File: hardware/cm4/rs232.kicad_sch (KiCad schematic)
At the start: 13 parts, among them J3 D340 PC (4P4C), U3 ADuM5211, U5 MAX3232E

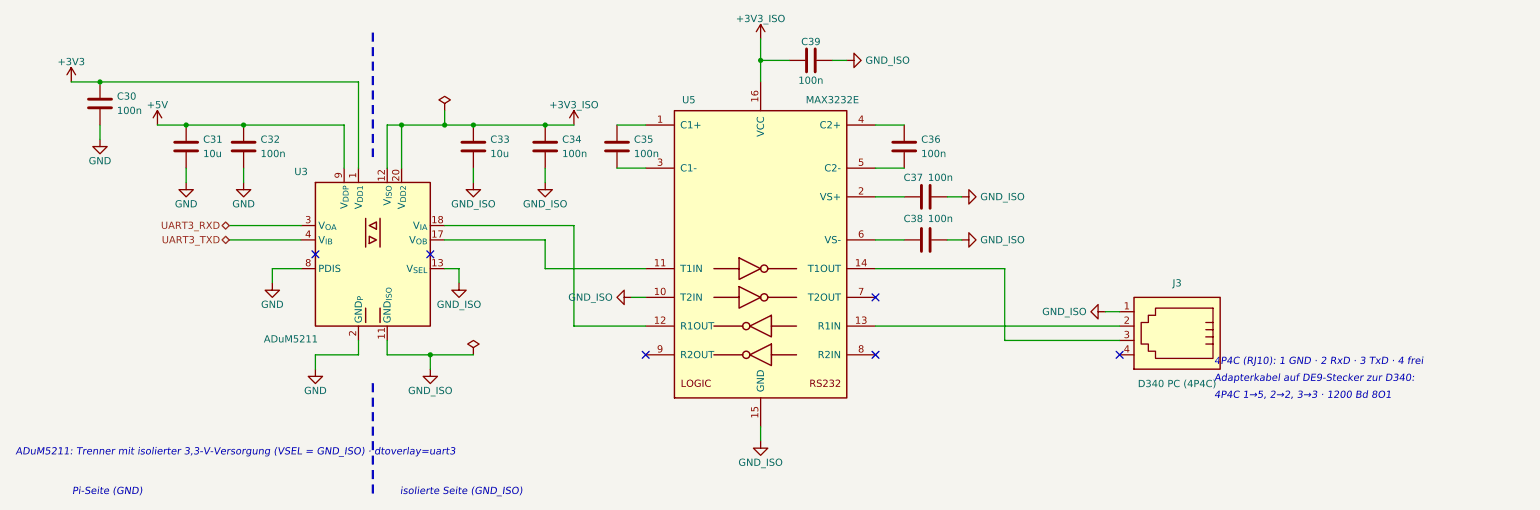
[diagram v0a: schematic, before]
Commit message: Schaltplan: Hinweise als Textkästen (KiCad bricht um); Texte werden in den Generator zurückgeführt
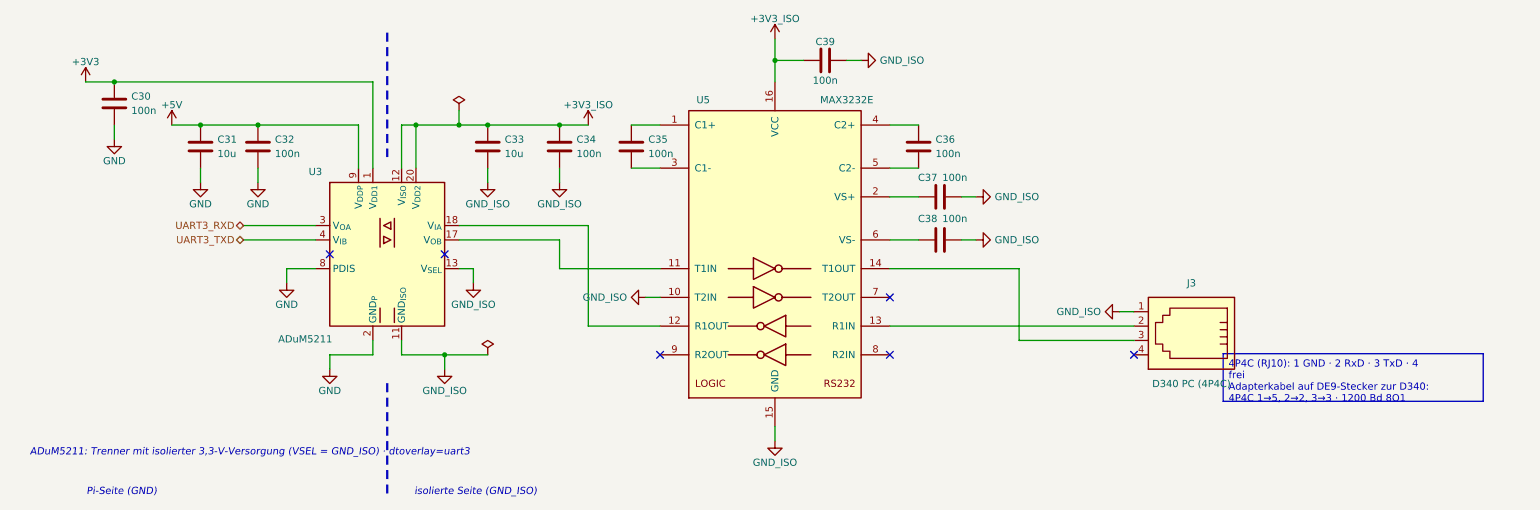
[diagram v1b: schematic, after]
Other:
- note removed: "4P4C (RJ10): 1 GND · 2 RxD · 3 TxD · 4 frei"
- note removed: "4P4C 1→5, 2→2, 3→3 · 1200 Bd 8O1"
- note removed: "Adapterkabel auf DE9-Stecker zur D340:"
- moved on the sheet: C30, C31, C32, C33, C34, C35, C36, C37, C38, C39, J3, U3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

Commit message: CM4-Schaltplan: Handänderungen übernommen (Handlage für 8 Blätter, 2 Texte zurückgeführt); Kastenhöhen aus gemessenen Zeichenbreiten
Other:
- note added: "ADuM5211: Trenner mit isolierter 3,3-V-Versorgung (VSEL = GND_ISO) dtoverlay=uart3"
- note removed: "ADuM5211: Trenner mit isolierter 3,3-V-Versorgung (VSEL = GND_ISO) · dtoverlay=uart3"
- moved on the sheet: C30, C31, C32, C33, C34, C35, C36, C37, C38, C39, J3, U3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
